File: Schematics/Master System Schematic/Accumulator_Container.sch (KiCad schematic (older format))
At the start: 24 parts, among them J1 Shutdown/Precharge Connector, J2 TSAL Connector, J3 Main TS Connector, J4 IMD/TSMP Connector, K1 SPST-NO (Precharge), K2 SPST-NO (AIR), K3 SPST-NO (AIR), K4 SPST-NC (Discharge), K5 SPDT (Precharge Control), SW1 HVD, SW2 SMD, SW3 SMD, U1 TSAL_ISOLATION

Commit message: Cleanup and general fixes
>Added TSAL circuit sheet
>Added project files for each sheet (kicad makes them automatically so might as well have them for editing indivudual sheets)
>Cleaned up wire runs
>Added LED as stand in for TSAL
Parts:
- removed U1: TSAL_ISOLATION, symbol NER:TSAL_ISOLATION
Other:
- moved on the sheet: J2
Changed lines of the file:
@@
 $Descr B 17000 11000
 encoding utf-8
-Sheet 4 10
+Sheet 4 11
 Title "Accumulator Container"
 Date "2020-09-17"
@@
 $EndDescr
 $Comp
-L NER:TSAL_ISOLATION U1
-U 1 1 5E5145FA
-P 10650 5750
-AR Path="/5E5145FA" Ref="U1"  Part="1"
-AR Path="/5F45B05E/5E5145FA" Ref="U1"  Part="1"
-F 0 "U1" H 10675 5865 50  0000 C CNN
-F 1 "TSAL_ISOLATION" H 10650 5800 50  0000 C CNN
-F 2 "" H 10650 5750 50  0001 C CNN
-F 3 "" H 10650 5750 50  0001 C CNN
-	1    10650 5750
-	1    0    0    -1
-$EndComp
-$Comp
 L Switch:SW_SPST SW1
 U 1 1 5E504806
@@
 L Connector:Conn_01x02_Female J2
 U 1 1 5F1E9418
-P 11950 5800
-F 0 "J2" H 11842 5985 50  0000 C CNN
-F 1 "TSAL Connector" H 11842 5894 50  0000 C CNN
-F 2 "" H 11950 5800 50  0001 C CNN
-F 3 "~" H 11950 5800 50  0001 C CNN
-	1    11950 5800
+P 12350 5800
+F 0 "J2" H 12242 5985 50  0000 C CNN
+F 1 "TSAL Connector" H 12242 5894 50  0000 C CNN
+F 2 "" H 12350 5800 50  0001 C CNN
+F 3 "~" H 12350 5800 50  0001 C CNN
+	1    12350 5800
 	-1   0    0    -1
 $EndComp
@@
 L Connector:Conn_01x02_Male J?
 U 1 1 5F1EC371
-P 11950 5800
-F 0 "J?" H 11922 5728 50  0001 R CNN
-F 1 "Conn_01x02_Male" H 11922 5683 50  0001 R CNN
-F 2 "" H 11950 5800 50  0001 C CNN
-F 3 "~" H 11950 5800 50  0001 C CNN
-	1    11950 5800
+P 12350 5800
+F 0 "J?" H 12322 5728 50  0001 R CNN
+F 1 "Conn_01x02_Male" H 12322 5683 50  0001 R CNN
+F 2 "" H 12350 5800 50  0001 C CNN
+F 3 "~" H 12350 5800 50  0001 C CNN
+	1    12350 5800
 	-1   0    0    -1
 $EndComp
@@
 Text Label 8900 6450 0    50   ~ 0
 12_2
-Text Label 11150 5800 0    50   ~ 0
+Text Label 11550 5800 0    50   ~ 0
 21_20
-Text Label 11150 5900 0    50   ~ 0
+Text Label 11550 5900 0    50   ~ 0
 22_20
 Text Label 7650 2200 0    50   ~ 0
@@
 Text HLabel 12500 4450 2    50   Output ~ 0
 TS-
-Text HLabel 12150 5800 2    50   Output ~ 0
+Text HLabel 12550 5800 2    50   Output ~ 0
 TSAL+
-Text HLabel 12150 5900 2    50   Output ~ 0
+Text HLabel 12550 5900 2    50   Output ~ 0
 TSAL-
 Text HLabel 12150 2600 2    50   Output ~ 0
@@
 Wire Wire Line
 	10350 4350 10350 4100
-Wire Wire Line
-	10300 5800 10250 5800
 Wire Wire Line
 	10250 5800 10250 4350
@@
 Wire Wire Line
 	10450 4100 10450 4450
-Wire Wire Line
-	10100 5900 10300 5900
 Connection ~ 10100 5900
 Wire Wire Line
@@
 	11100 4450 11750 4450
 Wire Wire Line
-	11000 5900 11750 5900
-Wire Wire Line
-	11000 5800 11750 5800
-Wire Wire Line
 	11100 2600 11750 2600
 Wire Wire Line
@@
 Wire Wire Line
 	10450 2500 11750 2500
+$Sheet
+S 10500 5700 700  300
+U 5FAAF22F
+F0 "TSAL_Circuit" 50
+F1 "TSAL_Circuit.sch" 50
+F2 "TS+" I L 10500 5800 50
+F3 "TS-" I L 10500 5900 50
+F4 "TSAL+" I R 11200 5800 50
+F5 "TSAL-" I R 11200 5900 50
+$EndSheet
+Wire Wire Line
+	10250 5800 10500 5800
+Wire Wire Line
+	10100 5900 10500 5900
+Wire Wire Line
+	11200 5800 12150 5800
+Wire Wire Line
+	11200 5900 12150 5900
 Wire Bus Line
 	1850 1900 1850 3750

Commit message: Created new MC interface
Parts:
- removed K5: SPDT (Precharge Control), Relay_THT:Relay_StandexMeder_DIP_LowProfile, symbol Relay:DIPxx-1Cxx-51x
- added K?: SPST-NO (AIR Control), Relay_THT:Relay_StandexMeder_DIP_LowProfile, symbol Relay:DIPxx-1Axx-11x
- added K?: SPST-NO (Precharge Control), Relay_THT:Relay_StandexMeder_DIP_LowProfile, symbol Relay:DIPxx-1Axx-11x
- J1: symbol Connector:Conn_01x04_Female -> Connector:Conn_01x06_Female
- J?: symbol Connector:Conn_01x04_Male -> Connector:Conn_01x06_Male
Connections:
- net 26_20: now also K?.7, K?.7, K?.8, K?.8
- net 27_20: now also K?.1, K?.14
- net 28_20: now also K?.1, K?.14
- net at J?.1 (Pin_1): now also K?.6
- net at J?.2 (Pin_2): now also K?.2
- net MotorController_Precharge_+ renamed MotorController_Precharge+
- net MotorController_Precharge_- renamed MotorController_Precharge-
- net MotorController_Precharge-: now also J1.5 (Pin_5)
- new net: J?.5 (Pin_5), K?.6
- new net: J?.6 (Pin_6), K?.2
- new net MotorController_AIR+: J1.6 (Pin_6)
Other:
- note added: "MC Control Relay PCB"
- moved on the sheet: F1, F2, F3, J2, J3, J4, K1, K2, K3, K4, R1, R2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

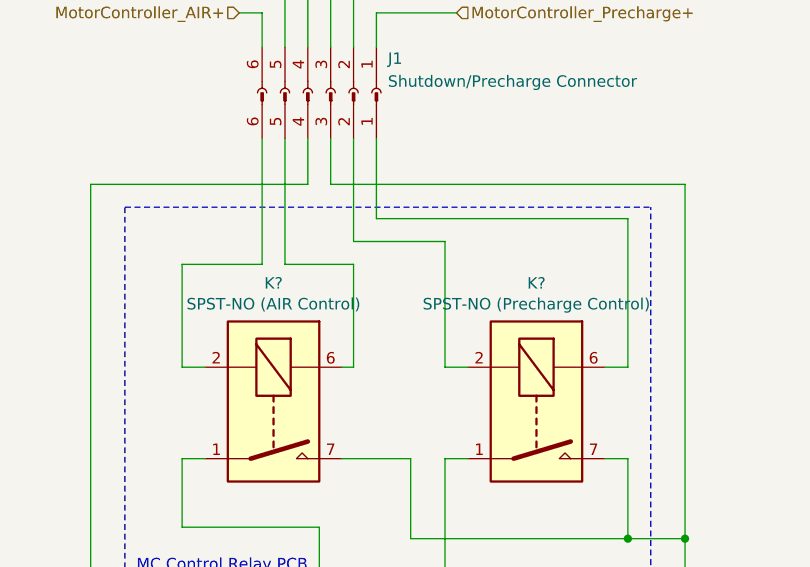
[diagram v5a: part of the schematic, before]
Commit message: Component IDs
Assigned remaining missing numbers
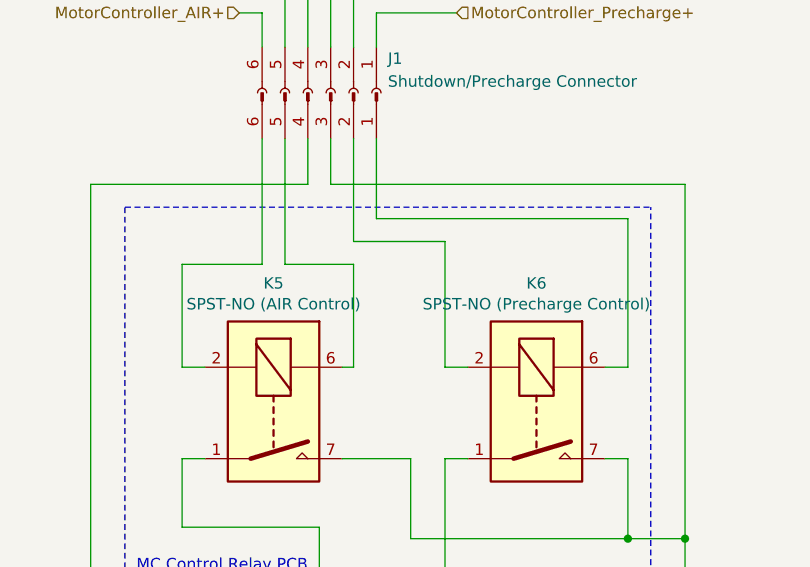
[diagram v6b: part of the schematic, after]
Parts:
- gave numbers to parts that had none: 6
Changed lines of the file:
@@
 $EndComp
 $Comp
-L Connector:Conn_01x02_Male J?
+L Connector:Conn_01x02_Male J8
 U 1 1 5F1EC371
 P 13600 7350
-F 0 "J?" H 13572 7278 50  0001 R CNN
+F 0 "J8" H 13572 7278 50  0001 R CNN
 F 1 "Conn_01x02_Male" H 13572 7233 50  0001 R CNN
 F 2 "" H 13600 7350 50  0001 C CNN
@@
 $EndComp
 $Comp
-L Connector:Conn_01x02_Male J?
+L Connector:Conn_01x02_Male J7
 U 1 1 5F1EE03B
 P 13200 5900
-F 0 "J?" H 13172 5874 50  0001 R CNN
+F 0 "J7" H 13172 5874 50  0001 R CNN
 F 1 "Conn_01x02_Male" H 13172 5828 50  0001 R CNN
 F 2 "" H 13200 5900 50  0001 C CNN
@@
 $EndComp
 $Comp
-L Connector:Conn_01x06_Male J?
+L Connector:Conn_01x06_Male J5
 U 1 1 5F2FD6BE
 P 9050 1550
-F 0 "J?" V 9112 1694 50  0001 L CNN
+F 0 "J5" V 9112 1694 50  0001 L CNN
 F 1 "Conn_01x04_Male" V 9158 1694 50  0001 L CNN
 F 2 "" H 9050 1550 50  0001 C CNN
@@
 TSMP+
 $Comp
-L Connector:Conn_01x04_Male J?
+L Connector:Conn_01x04_Male J6
 U 1 1 5F154419
 P 13200 4050
-F 0 "J?" H 13172 3978 50  0001 R CNN
+F 0 "J6" H 13172 3978 50  0001 R CNN
 F 1 "Conn_01x04_Male" H 13172 3933 50  0001 R CNN
 F 2 "" H 13200 4050 50  0001 C CNN
@@
 	12450 7450 13400 7450
 $Comp
-L Relay:DIPxx-1Axx-11x K?
+L Relay:DIPxx-1Axx-11x K5
 U 1 1 5F80B7CF
 P 8800 2950
-F 0 "K?" V 8233 2950 50  0000 C CNN
+F 0 "K5" V 8233 2950 50  0000 C CNN
 F 1 "SPST-NO (AIR Control)" V 8324 2950 50  0000 C CNN
 F 2 "Relay_THT:Relay_StandexMeder_DIP_LowProfile" H 9150 2900 50  0001 L CNN
@@
 $EndComp
 $Comp
-L Relay:DIPxx-1Axx-11x K?
+L Relay:DIPxx-1Axx-11x K6
 U 1 1 5F814F76
 P 9950 2950
-F 0 "K?" V 9383 2950 50  0000 C CNN
+F 0 "K6" V 9383 2950 50  0000 C CNN
 F 1 "SPST-NO (Precharge Control)" V 9474 2950 50  0000 C CNN
 F 2 "Relay_THT:Relay_StandexMeder_DIP_LowProfile" H 10300 2900 50  0001 L CNN
